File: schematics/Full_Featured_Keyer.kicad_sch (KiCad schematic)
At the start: 24 parts, among them J1 Straight Key in, J2 Paddles in, J3 FSK out, J3 PTT out, J3 TBD, J3 TX Keying in, Q2 2N2222, U1 LTV-847

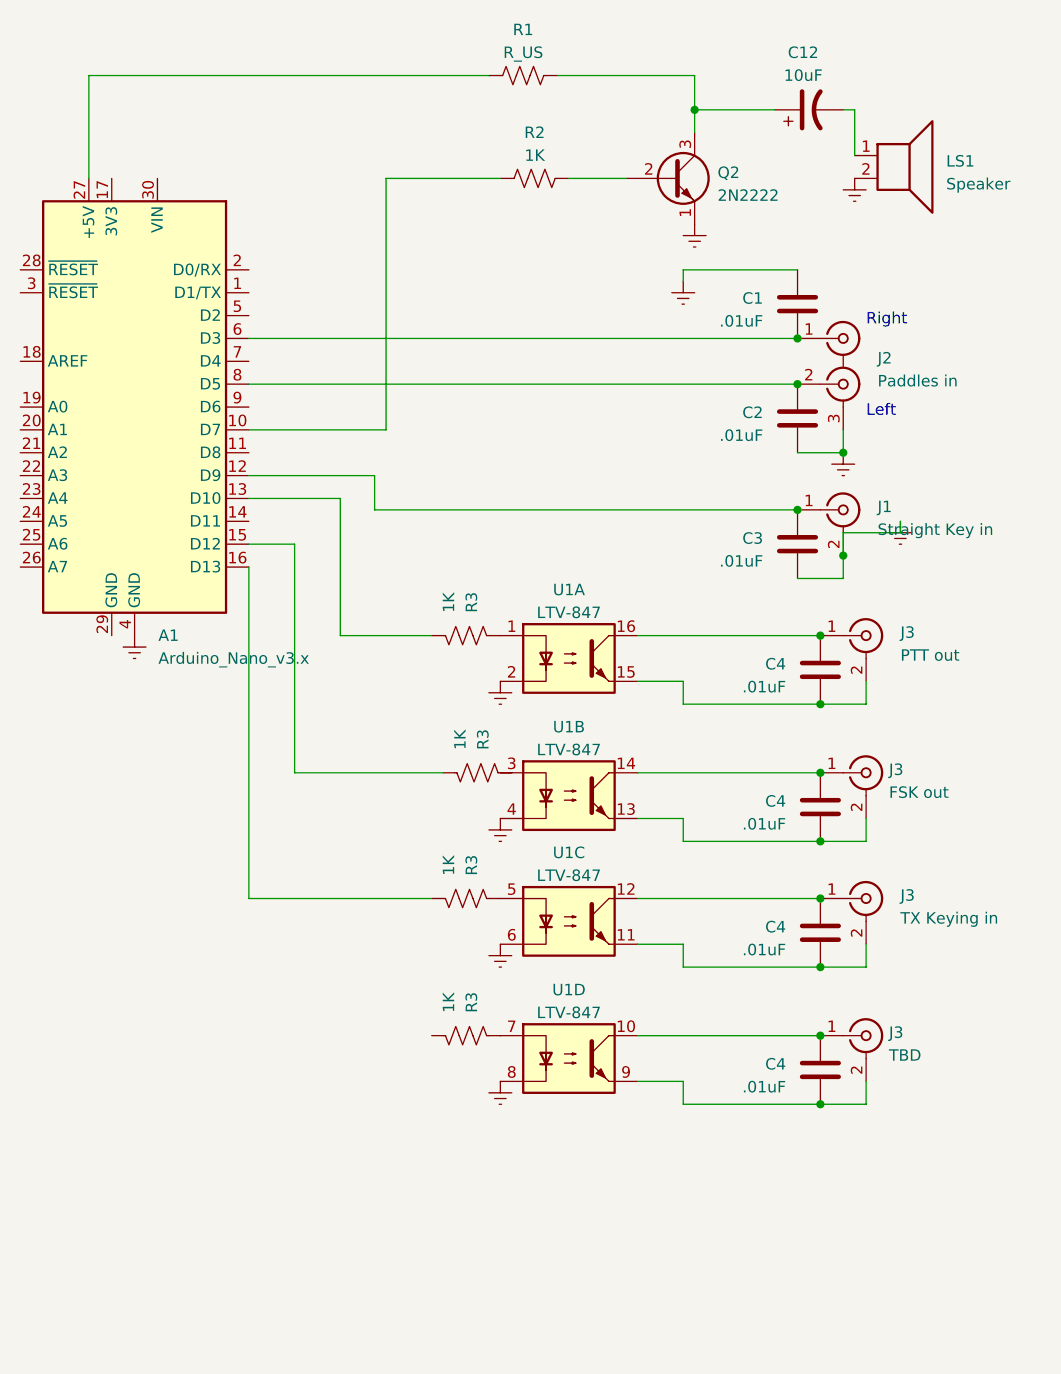
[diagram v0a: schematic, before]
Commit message: Ported to ESp32
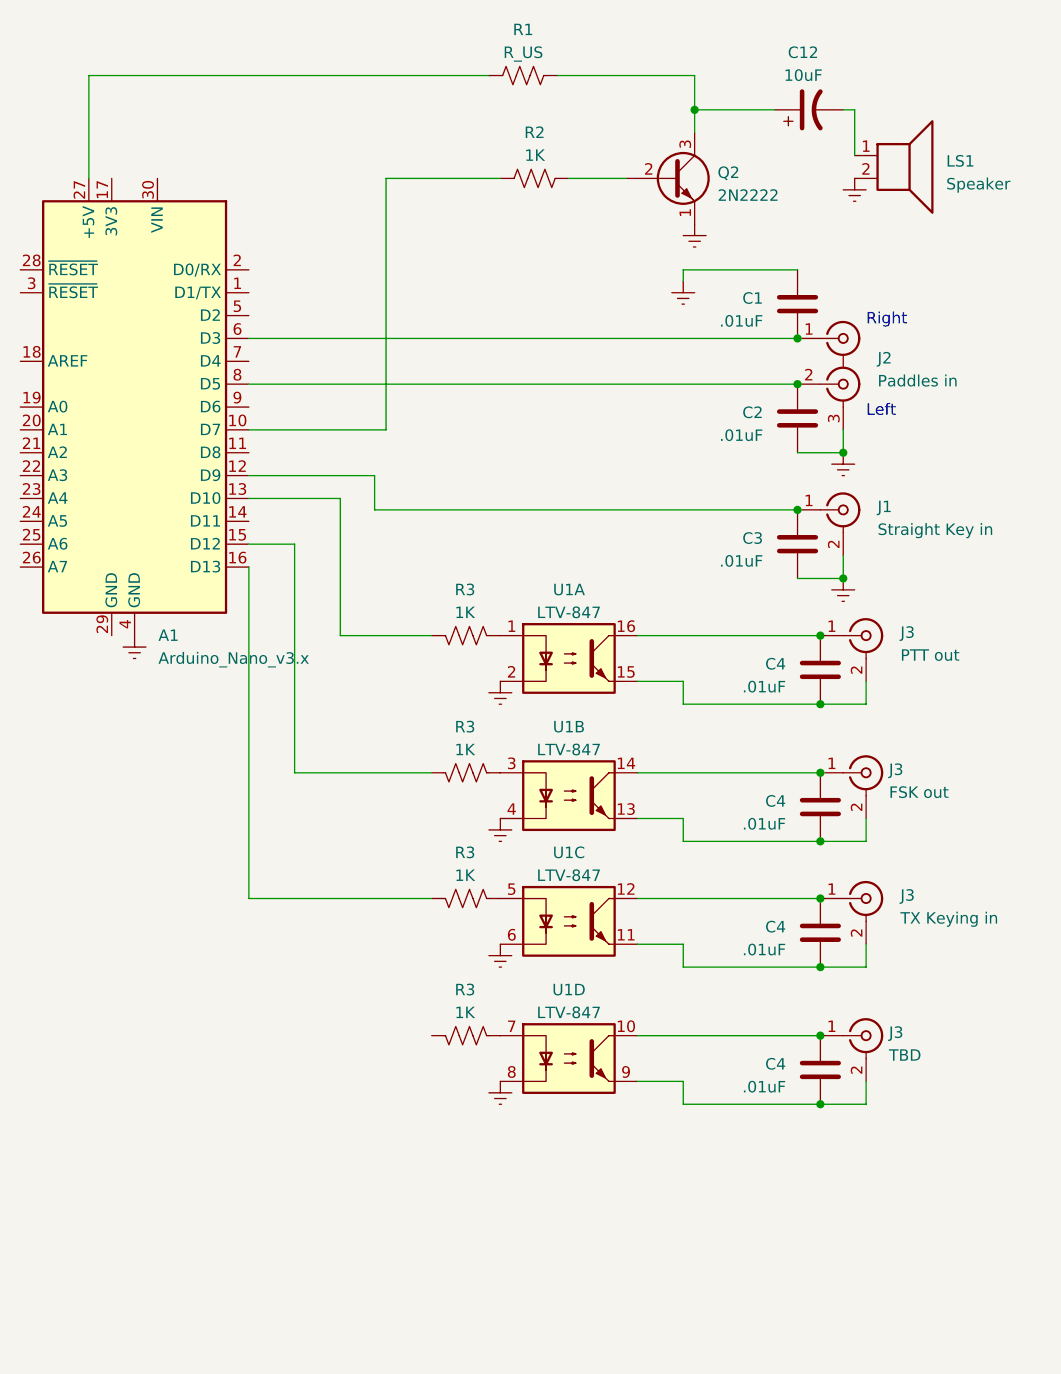
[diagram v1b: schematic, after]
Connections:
- net at U1.3: now also R3.1
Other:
- moved on the sheet: R3
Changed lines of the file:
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@@
   (junction (at 163.83 128.27) (diameter 0) (color 0 0 0 0)
   )
+  (junction (at 166.37 77.47) (diameter 0) (color 0 0 0 0)
+  )
   (junction (at 161.29 69.85) (diameter 0) (color 0 0 0 0)
   )
@@
   (junction (at 161.29 55.88) (diameter 0) (color 0 0 0 0)
   )
-  (junction (at 166.37 74.93) (diameter 0) (color 0 0 0 0)
-  )
   (junction (at 163.83 83.82) (diameter 0) (color 0 0 0 0)
   )
@@
     (stroke (width 0) (type default))
   )
-  (wire (pts (xy 172.72 72.39) (xy 166.37 72.39))
-    (stroke (width 0) (type default))
-  )
-  (wire (pts (xy 172.72 71.12) (xy 172.72 72.39))
-    (stroke (width 0) (type default))
-  )
   (wire (pts (xy 167.64 25.4) (xy 167.64 30.48))
     (stroke (width 0) (type default))
@@
     (stroke (width 0) (type default))
   )
-  (wire (pts (xy 105.41 99.06) (xy 121.92 99.06))
+  (wire (pts (xy 105.41 99.06) (xy 120.65 99.06))
     (stroke (width 0) (type default))
   )
@@
     (stroke (width 0) (type default))
   )
-  (wire (pts (xy 166.37 77.47) (xy 166.37 74.93))
-    (stroke (width 0) (type default))
-  )
   (wire (pts (xy 114.3 69.85) (xy 161.29 69.85))
     (stroke (width 0) (type default))
@@
     (stroke (width 0) (type default))
   )
-  (wire (pts (xy 166.37 72.39) (xy 166.37 74.93))
-    (stroke (width 0) (type default))
-  )
   (wire (pts (xy 163.83 91.44) (xy 168.91 91.44))
+    (stroke (width 0) (type default))
+  )
+  (wire (pts (xy 166.37 74.93) (xy 166.37 77.47))
     (stroke (width 0) (type default))
   )
@@
     )
   )
-  (symbol (lib_id "power:Earth") (at 172.72 71.12 0) (unit 1)
-    (in_bom yes) (on_board yes) (dnp no) (fields_autoplaced)
-    (property "Reference" "#PWR04" (at 172.72 77.47 0)
-      (effects (font (size 1.27 1.27)) hide)
-    )
-    (property "Value" "Earth" (at 172.72 74.93 0)
-      (effects (font (size 1.27 1.27)) hide)
-    )
-    (property "Footprint" "" (at 172.72 71.12 0)
-      (effects (font (size 1.27 1.27)) hide)
-    )
-    (property "Datasheet" "~" (at 172.72 71.12 0)
+  (symbol (lib_id "power:Earth") (at 166.37 77.47 0) (unit 1)
+    (in_bom yes) (on_board yes) (dnp no) (fields_autoplaced)
+    (property "Reference" "#PWR04" (at 166.37 83.82 0)
+      (effects (font (size 1.27 1.27)) hide)
+    )
+    (property "Value" "Earth" (at 166.37 81.28 0)
+      (effects (font (size 1.27 1.27)) hide)
+    )
+    (property "Footprint" "" (at 166.37 77.47 0)
+      (effects (font (size 1.27 1.27)) hide)
+    )
+    (property "Datasheet" "~" (at 166.37 77.47 0)
       (effects (font (size 1.27 1.27)) hide)
     )
@@
   (symbol (lib_id "Device:R_US") (at 124.46 128.27 270) (mirror x) (unit 1)
     (in_bom yes) (on_board yes) (dnp no)
-    (property "Reference" "R3" (at 125.095 125.73 0)
-      (effects (font (size 1.27 1.27)) (justify left))
-    )
-    (property "Value" "1K" (at 122.555 125.73 0)
+    (property "Reference" "R3" (at 123.19 123.19 90)
+      (effects (font (size 1.27 1.27)) (justify left))
+    )
+    (property "Value" "1K" (at 123.19 125.73 90)
       (effects (font (size 1.27 1.27)) (justify left))
     )
@@
   (symbol (lib_id "Device:R_US") (at 124.46 113.03 270) (mirror x) (unit 1)
     (in_bom yes) (on_board yes) (dnp no)
-    (property "Reference" "R3" (at 125.095 110.49 0)
-      (effects (font (size 1.27 1.27)) (justify left))
-    )
-    (property "Value" "1K" (at 122.555 110.49 0)
+    (property "Reference" "R3" (at 123.19 107.95 90)
+      (effects (font (size 1.27 1.27)) (justify left))
+    )
+    (property "Value" "1K" (at 123.19 110.49 90)
       (effects (font (size 1.27 1.27)) (justify left))
     )
@@
   (symbol (lib_id "Device:R_US") (at 124.46 83.82 270) (mirror x) (unit 1)
     (in_bom yes) (on_board yes) (dnp no)
-    (property "Reference" "R3" (at 125.095 81.28 0)
-      (effects (font (size 1.27 1.27)) (justify left))
-    )
-    (property "Value" "1K" (at 122.555 81.28 0)
+    (property "Reference" "R3" (at 123.19 78.74 90)
+      (effects (font (size 1.27 1.27)) (justify left))
+    )
+    (property "Value" "1K" (at 123.19 81.28 90)
       (effects (font (size 1.27 1.27)) (justify left))
     )
@@
     )
   )
-  (symbol (lib_id "Device:R_US") (at 125.73 99.06 270) (mirror x) (unit 1)
+  (symbol (lib_id "Device:R_US") (at 124.46 99.06 270) (mirror x) (unit 1)
     (in_bom yes) (on_board yes) (dnp no)
-    (property "Reference" "R3" (at 126.365 96.52 0)
-      (effects (font (size 1.27 1.27)) (justify left))
-    )
-    (property "Value" "1K" (at 123.825 96.52 0)
-      (effects (font (size 1.27 1.27)) (justify left))
-    )
-    (property "Footprint" "" (at 125.476 98.044 90)
-      (effects (font (size 1.27 1.27)) hide)
-    )
-    (property "Datasheet" "~" (at 125.73 99.06 0)
-      (effects (font (size 1.27 1.27)) hide)
-    )
+    (property "Reference" "R3" (at 123.19 93.98 90)
+      (effects (font (size 1.27 1.27)) (justify left))
+    )
+    (property "Value" "1K" (at 123.19 96.52 90)
+      (effects (font (size 1.27 1.27)) (justify left))
+    )
+    (property "Footprint" "" (at 124.206 98.044 90)
+      (effects (font (size 1.27 1.27)) hide)
+    )
+    (property "Datasheet" "~" (at 124.46 99.06 0)
+      (effects (font (size 1.27 1.27)) hide)
+    )

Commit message: Updates
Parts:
- removed C4: .01uF, symbol Device:C
- removed J3: TBD, symbol Connector:Conn_Coaxial
- removed R3: 1K, symbol Device:R_US
- added BZ1: Buzzer, symbol Device:Buzzer
- J3: value TX Keying in -> TX Keying out
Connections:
- net Earth: now also BZ1.2 (+)
- net at C4.2, J3.2 (Ext): now also U1.15; no longer U1.11
- net at C4.1, J3.1 (In): now also U1.16; no longer U1.12
- net at R3.1: now also U1.1; no longer U1.5
- net at R3.1: now also U1.5; no longer U1.1
- net at C4.2, J3.2 (Ext): now also U1.11; no longer U1.15
- net at C4.1, J3.1 (In): now also U1.12; no longer U1.16
- net at A1.14 (D11): now also BZ1.1 (-)
